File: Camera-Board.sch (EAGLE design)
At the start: 65 parts, among them J1 RJ45KEYSTONE-942, J2 JTAG_ARM_10PIN, J3 APP_2POS_CONFIG12V_HORIZ, J8 APPPP45_PCB_HORIZ_RIGHT, U1 TM4C1294NCPDT, U2 HX1198FNL, U3 SLVU2.8-4, U4 OKI-78SR-5/1.5-W36HC, U5 TPS73733DCQ, U7 OKI-78SR-5/1.5-W36HC, Y1 NX3225GA, Y2 CRYATL_32K_SMD

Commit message: Added Max4312 chip to schematic
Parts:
- added R20, R21, R22, R23: 500, resistor:R-US_R0603
- added R24: 75, resistor:R-US_R0603
- added U6, U8: MAX4312ESE, MRDT-ICs:MAX4312ESE
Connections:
- new net CAM_IN0: R24.2, U6.IN0, U8.IN0
- new net CAM_IN1: U6.IN1, U8.IN1
- new net CAM_IN2: U6.IN2, U8.IN2
- new net CAM_IN3: U6.IN3, U8.IN3
- new net CAM_IN4: U6.IN4, U8.IN4
- new net CAM_IN5: U6.IN5, U8.IN5
- new net CAM_IN6: U6.IN6, U8.IN6
- new net CAM_IN7: U6.IN7, U8.IN7
- new net CAM_OUT0: R20.2, U6.OUT
- new net CAM_OUT1: R22.2, U8.OUT
- new net MUX0_0: U6.A0
- new net MUX0_1: U6.A1
- new net MUX0_2: U6.A2
- new net MUX0_SHDN: U6.!SHDN
- new net MUX1_0: U8.A0
- new net MUX1_1: U8.A1
- new net MUX1_2: U8.A2
- new net MUX1_SHDN: U8.!SHDN
- new net N$1: R20.1, R21.2, U6.FB
- new net N$2: R22.1, R23.2, U8.FB
- net +5V_LOGIC: now also U6.VCC, U8.VCC
- net GND: now also R21.1, R23.1, R24.1, U6.VEE, U8.VEE

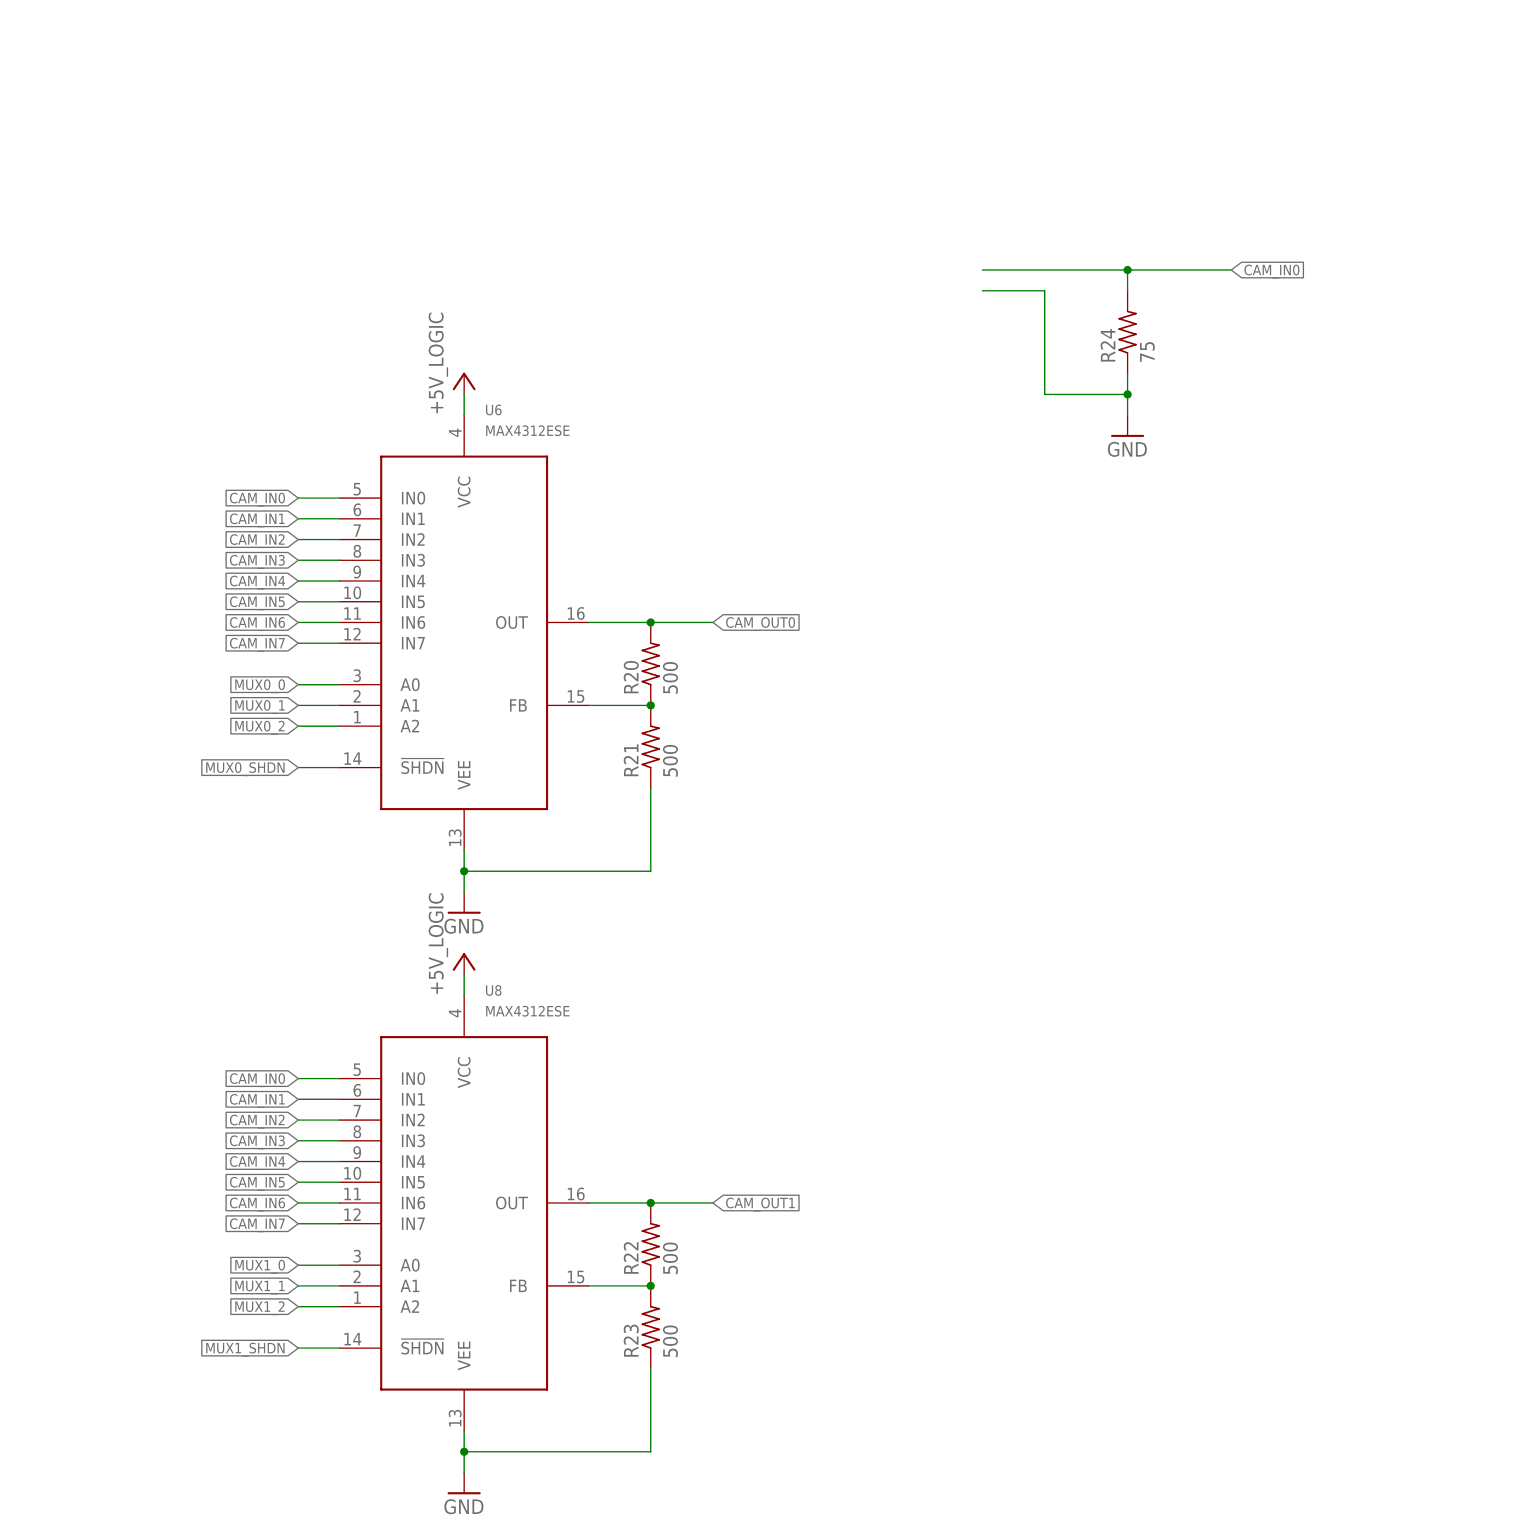
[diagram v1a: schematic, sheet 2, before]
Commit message: Added Input and Output Connectors
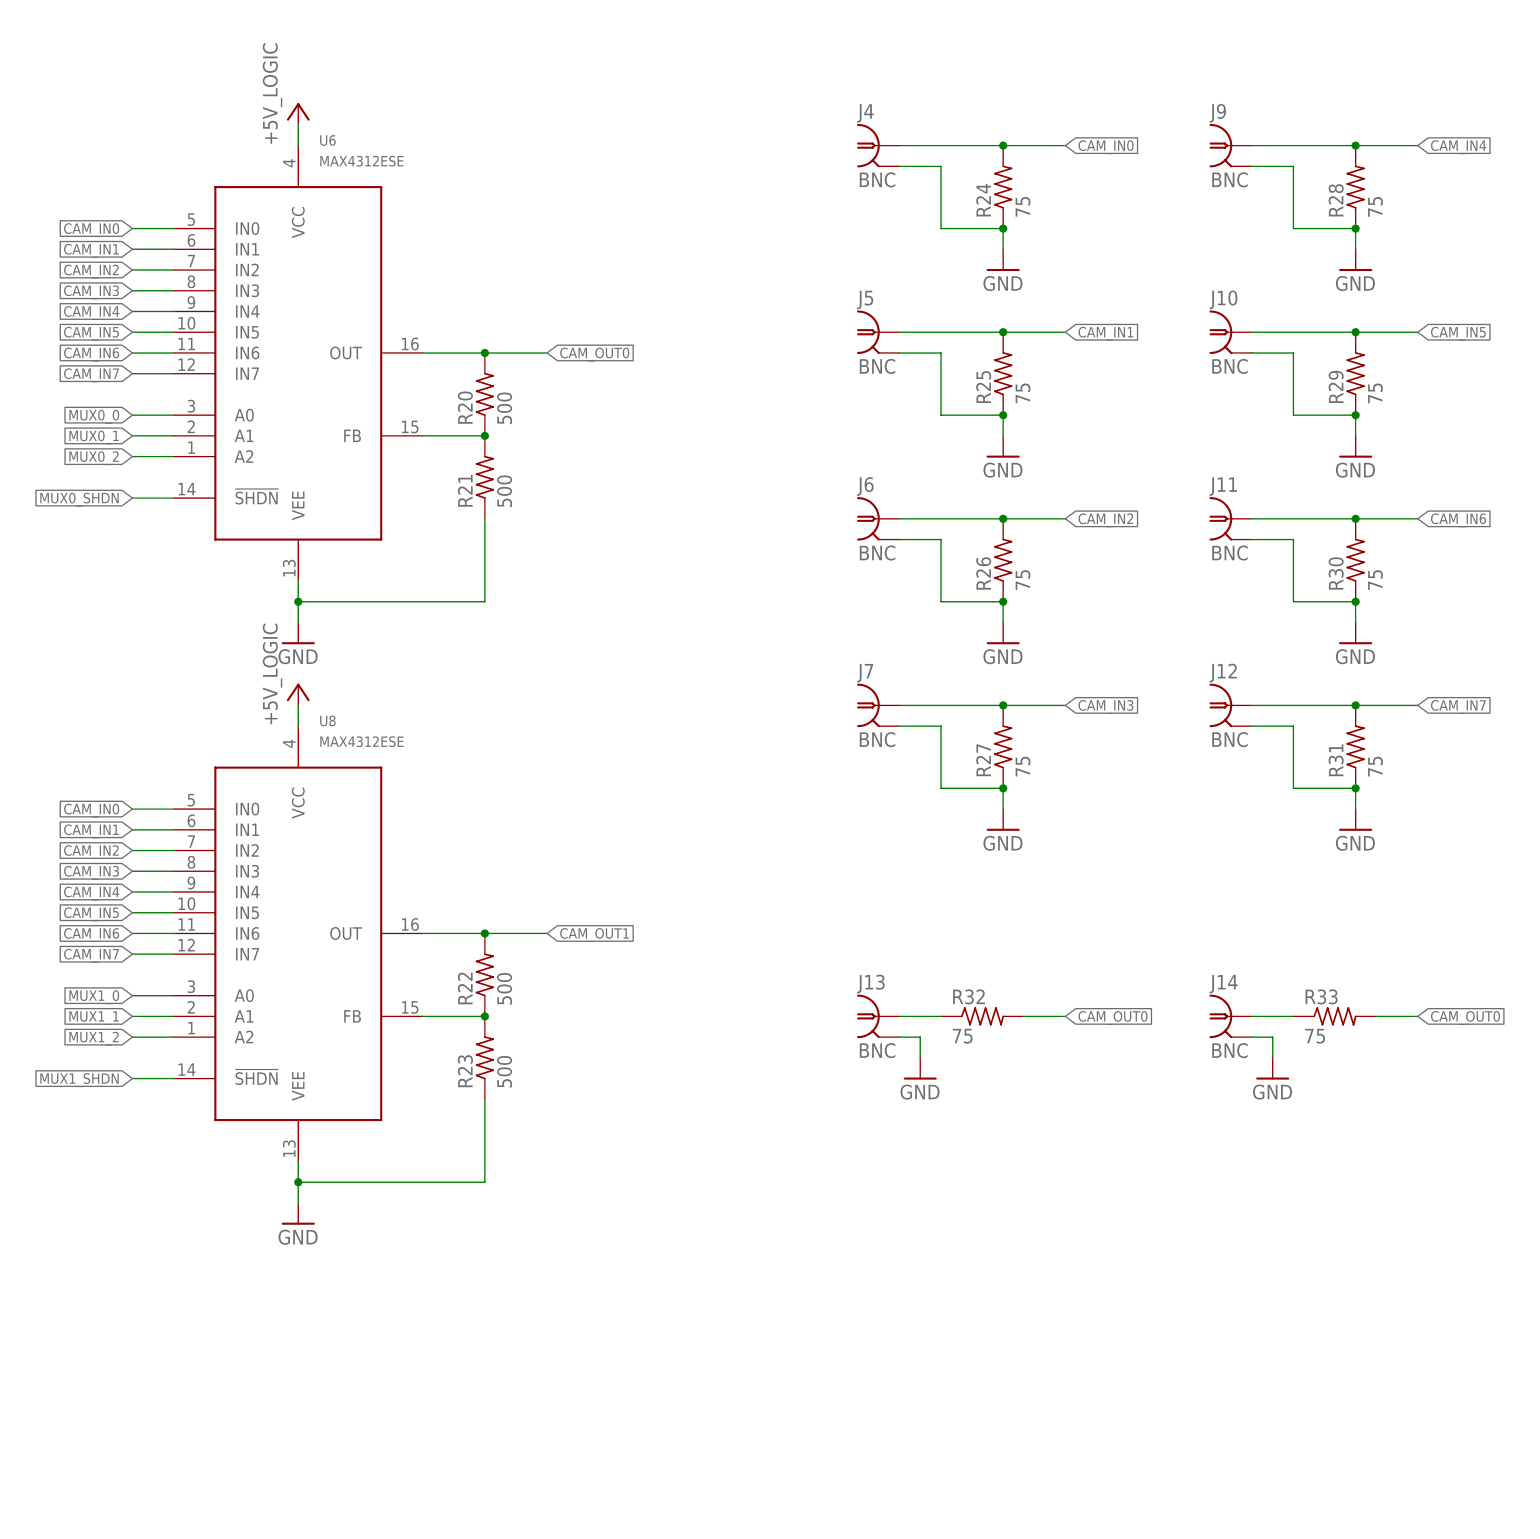
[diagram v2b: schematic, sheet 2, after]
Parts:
- added J10, J11, J12, J13, J14, J4, J5, J6, J7, J9: BNC, MRDT-Connectors:BNC
- added R25, R26, R27, R28, R29, R30, R31, R32, R33: 75, resistor:R-US_R0603
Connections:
- new net N$3: J14.1, R33.1
- new net N$4: J13.1, R32.1
- net CAM_IN0: now also J4.1
- net CAM_IN1: now also J5.1, R25.2
- net CAM_IN2: now also J6.1, R26.2
- net CAM_IN3: now also J7.1, R27.2
- net CAM_IN4: now also J9.1, R28.2
- net CAM_IN5: now also J10.1, R29.2
- net CAM_IN6: now also J11.1, R30.2
- net CAM_IN7: now also J12.1, R31.2
- net CAM_OUT0: now also R32.2, R33.2
- net GND: now also J10.2, J11.2, J12.2, J13.2, J14.2, J4.2, J5.2, J6.2, J7.2, J9.2, R25.1, R26.1, R27.1, R28.1, R29.1, R30.1, R31.1
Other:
- moved on the sheet: R20, R21, R22, R23, R24, U6, U8

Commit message: Rotouted most connections
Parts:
- removed C25, C26: 10uF, resistor:C-USC1206
- removed J8: APPPP45_PCB_HORIZ_RIGHT, MRDT-Connectors:APPPP45_PCB_HORIZ_RIGHT
- removed U7: OKI-78SR-5/1.5-W36HC, MRDT-ICs:OKI-78SR-5/1.5-W36HC
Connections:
- removed net +12V_ACT: C25.1, J8.P$1, U7.VI
- removed net +5V_ACT: C26.1, U7.VO
- net CAM_OUT0: no longer R33.2
- net CAM_OUT1: now also R33.2
- net GND: no longer C25.2, C26.2, U7.GND
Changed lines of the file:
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@@
 <part name="GND20" library="supply1" deviceset="GND" device=""/>
 <part name="S1" library="MRDT-UserInput" deviceset="SWITCH_TACTILE" device=""/>
-<part name="J8" library="MRDT-Connectors" deviceset="APP" device="PP45_PCB_HORIZ_RIGHT"/>
-<part name="P+6" library="supply1" deviceset="+12V" device="" value="+12V_ACT"/>
-<part name="U7" library="MRDT-ICs" deviceset="OKI-78SR-*/1.5-W36?C" device="H" technology="5"/>
-<part name="P+7" library="supply1" deviceset="+12V" device="" value="+12V_ACT"/>
-<part name="GND23" library="supply1" deviceset="GND" device=""/>
-<part name="C25" library="resistor" deviceset="C-US" device="C1206" value="10uF"/>
-<part name="C26" library="resistor" deviceset="C-US" device="C1206" value="10uF"/>
-<part name="P+8" library="supply1" deviceset="+5V" device="" value="+5V_ACT"/>
 <part name="U6" library="MRDT-ICs" deviceset="MAX4312E?E" device="S"/>
 <part name="P+4" library="supply1" deviceset="+5V" device="" value="+5V_LOGIC"/>
@@
 <instance part="GND20" gate="1" x="271.78" y="12.7"/>
 <instance part="S1" gate="G$1" x="10.16" y="68.58" rot="R90"/>
-<instance part="J8" gate="G$1" x="281.94" y="27.94"/>
-<instance part="P+6" gate="1" x="266.7" y="38.1"/>
-<instance part="U7" gate="G$1" x="198.12" y="66.04"/>
-<instance part="P+7" gate="1" x="182.88" y="76.2"/>
-<instance part="GND23" gate="1" x="200.66" y="45.72"/>
-<instance part="C25" gate="G$1" x="182.88" y="58.42"/>
-<instance part="C26" gate="G$1" x="215.9" y="58.42"/>
-<instance part="P+8" gate="1" x="215.9" y="76.2"/>
 </instances>
 <busses>
@@
 <wire x1="271.78" y1="17.78" x2="271.78" y2="15.24" width="0.1524" layer="91"/>
 </segment>
-<segment>
-<pinref part="GND23" gate="1" pin="GND"/>
-<pinref part="U7" gate="G$1" pin="GND"/>
-<wire x1="200.66" y1="48.26" x2="200.66" y2="50.8" width="0.1524" layer="91"/>
-<pinref part="C25" gate="G$1" pin="2"/>
-<wire x1="200.66" y1="50.8" x2="200.66" y2="58.42" width="0.1524" layer="91"/>
-<wire x1="182.88" y1="53.34" x2="182.88" y2="50.8" width="0.1524" layer="91"/>
-<wire x1="182.88" y1="50.8" x2="200.66" y2="50.8" width="0.1524" layer="91"/>
-<junction x="200.66" y="50.8"/>
-<pinref part="C26" gate="G$1" pin="2"/>
-<wire x1="215.9" y1="53.34" x2="215.9" y2="50.8" width="0.1524" layer="91"/>
-<wire x1="215.9" y1="50.8" x2="200.66" y2="50.8" width="0.1524" layer="91"/>
-</segment>
 </net>
 <net name="N_$1" class="0">
@@
 </segment>
 </net>
-<net name="+12V_ACT" class="0">
-<segment>
-<pinref part="J8" gate="G$1" pin="P$1"/>
-<pinref part="P+6" gate="1" pin="+12V"/>
-<wire x1="274.32" y1="27.94" x2="266.7" y2="27.94" width="0.1524" layer="91"/>
-<wire x1="266.7" y1="27.94" x2="266.7" y2="35.56" width="0.1524" layer="91"/>
-</segment>
-<segment>
-<pinref part="U7" gate="G$1" pin="VI"/>
-<pinref part="P+7" gate="1" pin="+12V"/>
-<wire x1="190.5" y1="66.04" x2="182.88" y2="66.04" width="0.1524" layer="91"/>
-<wire x1="182.88" y1="66.04" x2="182.88" y2="73.66" width="0.1524" layer="91"/>
-<pinref part="C25" gate="G$1" pin="1"/>
-<wire x1="182.88" y1="60.96" x2="182.88" y2="66.04" width="0.1524" layer="91"/>
-<junction x="182.88" y="66.04"/>
-</segment>
-</net>
 <net name="+5V_LOGIC" class="0">
 <segment>
@@
 <wire x1="210.82" y1="116.84" x2="210.82" y2="127" width="0.1524" layer="91"/>
 <junction x="210.82" y="127"/>
-</segment>
-</net>
-<net name="+5V_ACT" class="0">
-<segment>
-<pinref part="C26" gate="G$1" pin="1"/>
-<pinref part="U7" gate="G$1" pin="VO"/>
-<wire x1="215.9" y1="60.96" x2="215.9" y2="66.04" width="0.1524" layer="91"/>
-<wire x1="215.9" y1="66.04" x2="210.82" y2="66.04" width="0.1524" layer="91"/>
-<pinref part="P+8" gate="1" pin="+5V"/>
-<wire x1="215.9" y1="66.04" x2="215.9" y2="73.66" width="0.1524" layer="91"/>
-<junction x="215.9" y="66.04"/>
 </segment>
 </net>
@@
 <label x="142.24" y="152.4" size="1.27" layer="95" xref="yes"/>
 </segment>
-<segment>
-<pinref part="R33" gate="G$1" pin="2"/>
-<wire x1="180.34" y1="152.4" x2="185.42" y2="152.4" width="0.1524" layer="91"/>
-<label x="185.42" y="152.4" size="1.27" layer="95" xref="yes"/>
-</segment>
 </net>
 <net name="N$1" class="0">
@@
 <junction x="71.12" y="162.56"/>
 </segment>
-</net>
+<segment>
+<pinref part="R33" gate="G$1" pin="2"/>
+<wire x1="180.34" y1="152.4" x2="185.42" y2="152.4" width="0.1524" layer="91"/>
+<label x="185.42" y="152.4" size="1.27" layer="95" xref="yes"/>
+</segment>
+</net>

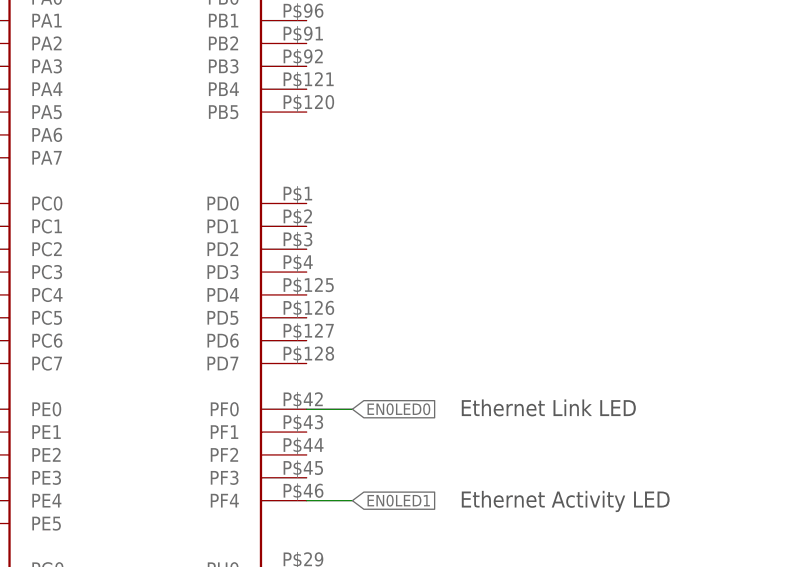
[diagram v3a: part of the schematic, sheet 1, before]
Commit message: Finished routing board
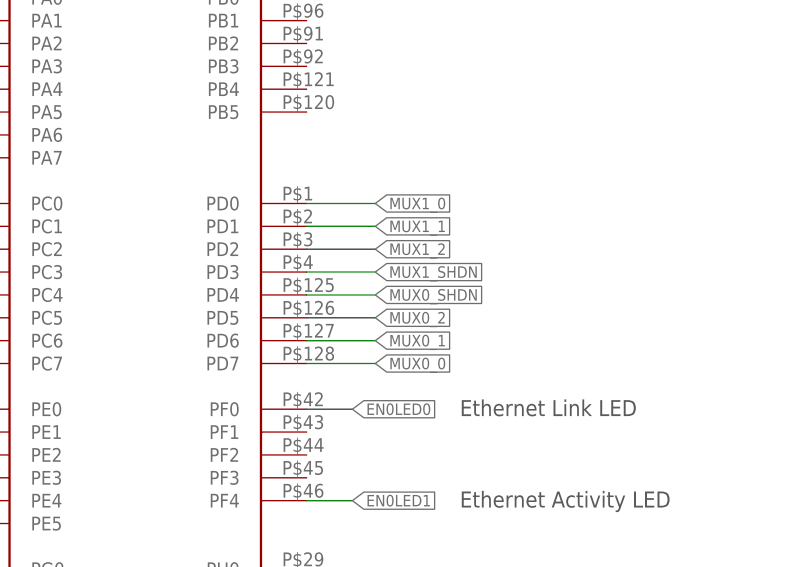
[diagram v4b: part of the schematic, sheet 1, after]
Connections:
- net MUX0_0: now also U1G$1.PD7@128
- net MUX0_1: now also U1G$1.PD6@127
- net MUX0_2: now also U1G$1.PD5@126
- net MUX0_SHDN: now also U1G$1.PD4@125
- net MUX1_0: now also U1G$1.PD0@1
- net MUX1_1: now also U1G$1.PD1@2
- net MUX1_2: now also U1G$1.PD2@3
- net MUX1_SHDN: now also U1G$1.PD3@4
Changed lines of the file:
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@@
+</segment>
+</net>
+<net name="MUX0_SHDN" class="0">
+<segment>
+<pinref part="U1" gate="G$1" pin="PD4@125"/>
+<label x="111.76" y="226.06" size="1.27" layer="95" xref="yes"/>
+<wire x1="104.14" y1="226.06" x2="111.76" y2="226.06" width="0.1524" layer="91"/>
+</segment>
+</net>
+<net name="MUX0_2" class="0">
+<segment>
+<pinref part="U1" gate="G$1" pin="PD5@126"/>
+<label x="111.76" y="223.52" size="1.27" layer="95" xref="yes"/>
+<wire x1="104.14" y1="223.52" x2="111.76" y2="223.52" width="0.1524" layer="91"/>
+</segment>
+</net>
+<net name="MUX0_1" class="0">
+<segment>
+<pinref part="U1" gate="G$1" pin="PD6@127"/>
+<wire x1="104.14" y1="220.98" x2="111.76" y2="220.98" width="0.1524" layer="91"/>
+<label x="111.76" y="220.98" size="1.27" layer="95" xref="yes"/>
+</segment>
+</net>
+<net name="MUX0_0" class="0">
+<segment>
+<pinref part="U1" gate="G$1" pin="PD7@128"/>
+<wire x1="104.14" y1="218.44" x2="111.76" y2="218.44" width="0.1524" layer="91"/>
+<label x="111.76" y="218.44" size="1.27" layer="95" xref="yes"/>
+</segment>
+</net>
+<net name="MUX1_0" class="0">
+<segment>
+<pinref part="U1" gate="G$1" pin="PD0@1"/>
+<wire x1="104.14" y1="236.22" x2="111.76" y2="236.22" width="0.1524" layer="91"/>
+<label x="111.76" y="236.22" size="1.27" layer="95" xref="yes"/>
+</segment>
+</net>
+<net name="MUX1_1" class="0">
+<segment>
+<pinref part="U1" gate="G$1" pin="PD1@2"/>
+<wire x1="104.14" y1="233.68" x2="111.76" y2="233.68" width="0.1524" layer="91"/>
+<label x="111.76" y="233.68" size="1.27" layer="95" xref="yes"/>
+</segment>
+</net>
+<net name="MUX1_2" class="0">
+<segment>
+<pinref part="U1" gate="G$1" pin="PD2@3"/>
+<wire x1="104.14" y1="231.14" x2="111.76" y2="231.14" width="0.1524" layer="91"/>
+<label x="111.76" y="231.14" size="1.27" layer="95" xref="yes"/>
+</segment>
+</net>
+<net name="MUX1_SHDN" class="0">
+<segment>
+<pinref part="U1" gate="G$1" pin="PD3@4"/>
+<wire x1="104.14" y1="228.6" x2="111.76" y2="228.6" width="0.1524" layer="91"/>
+<label x="111.76" y="228.6" size="1.27" layer="95" xref="yes"/>
 </segment>
 </net>
